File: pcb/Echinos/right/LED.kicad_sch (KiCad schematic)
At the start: 14 parts

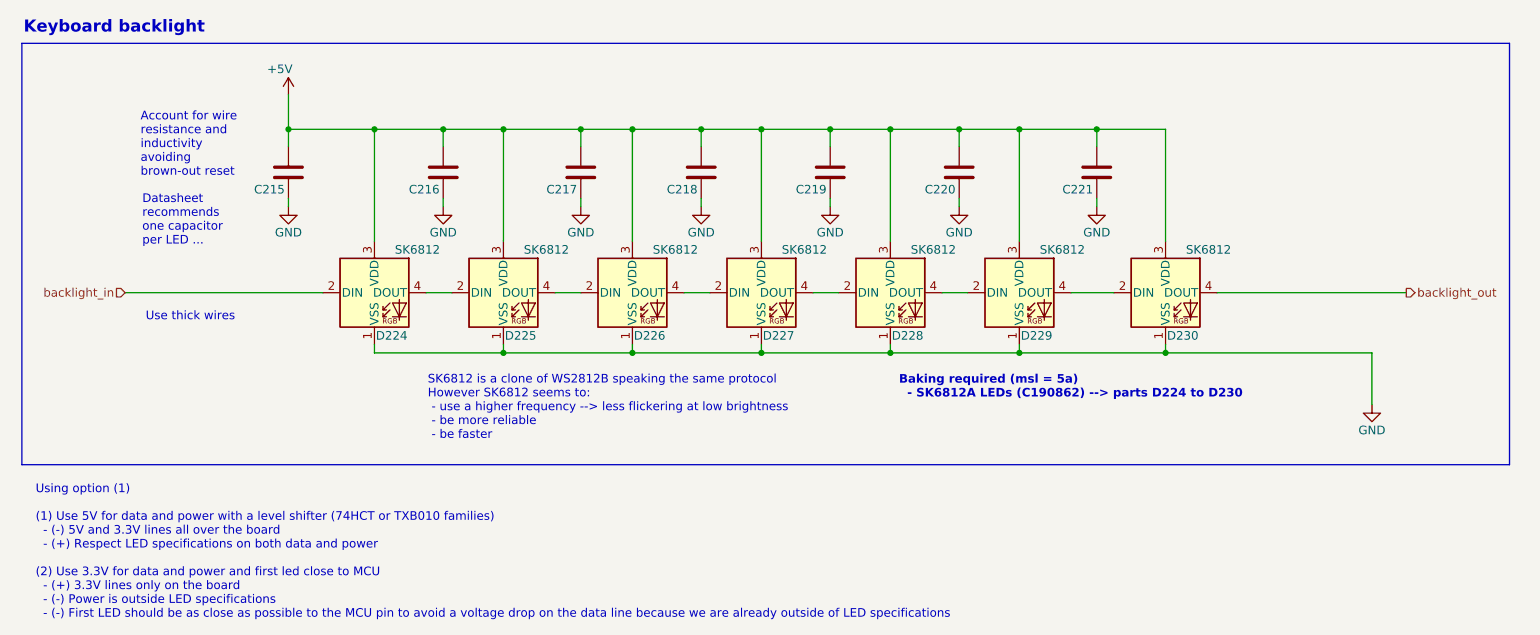
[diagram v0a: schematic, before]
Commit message: 💥 [PCB] - Group left and right on the same PCB.   - Schematics are different for each side   - Split trace naming to avoid mixing right and left   - Add mouse bite between both halves to make manufacturing easier (new footprint)
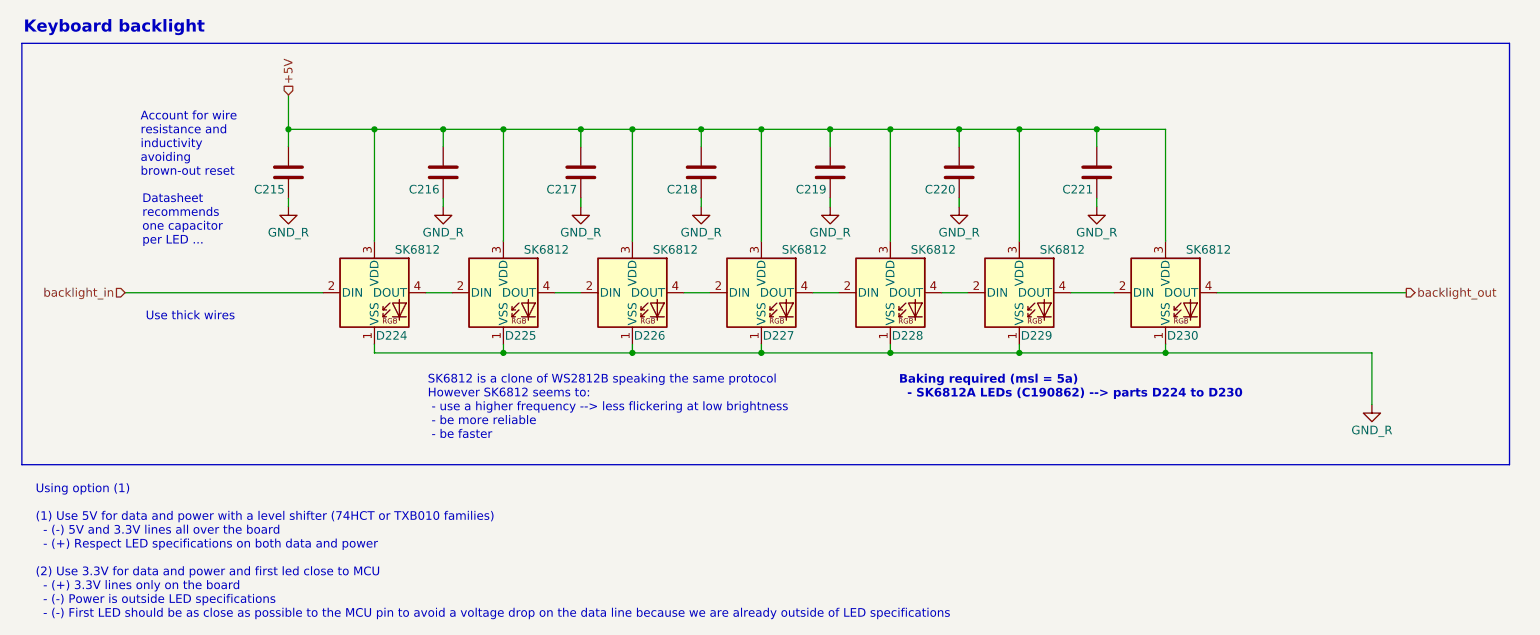
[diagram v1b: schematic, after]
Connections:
- net GND renamed GND_R
